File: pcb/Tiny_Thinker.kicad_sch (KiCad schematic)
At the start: 47 parts, among them J2 PERIPHERALS, J3 ADC_TIM, J8 USB_C_Receptacle_USB2.0_16P, SW1 SW_Push, SW2 SW_SPDT, U1 STM32F446RET6, U2 AMS1117-3.3, U3 TPS2116DRL, Y1 16MHz

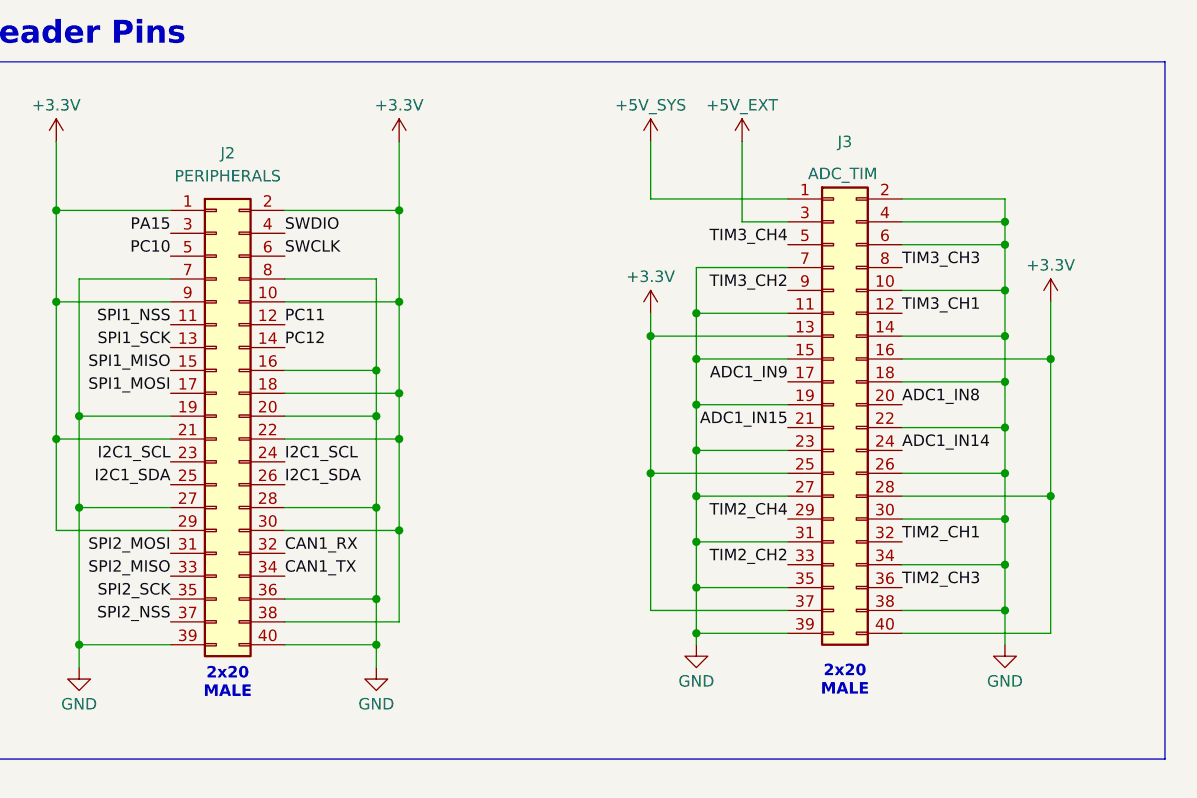
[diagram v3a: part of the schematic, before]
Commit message: renamed header connectors for BOM and connected NRST to a pin
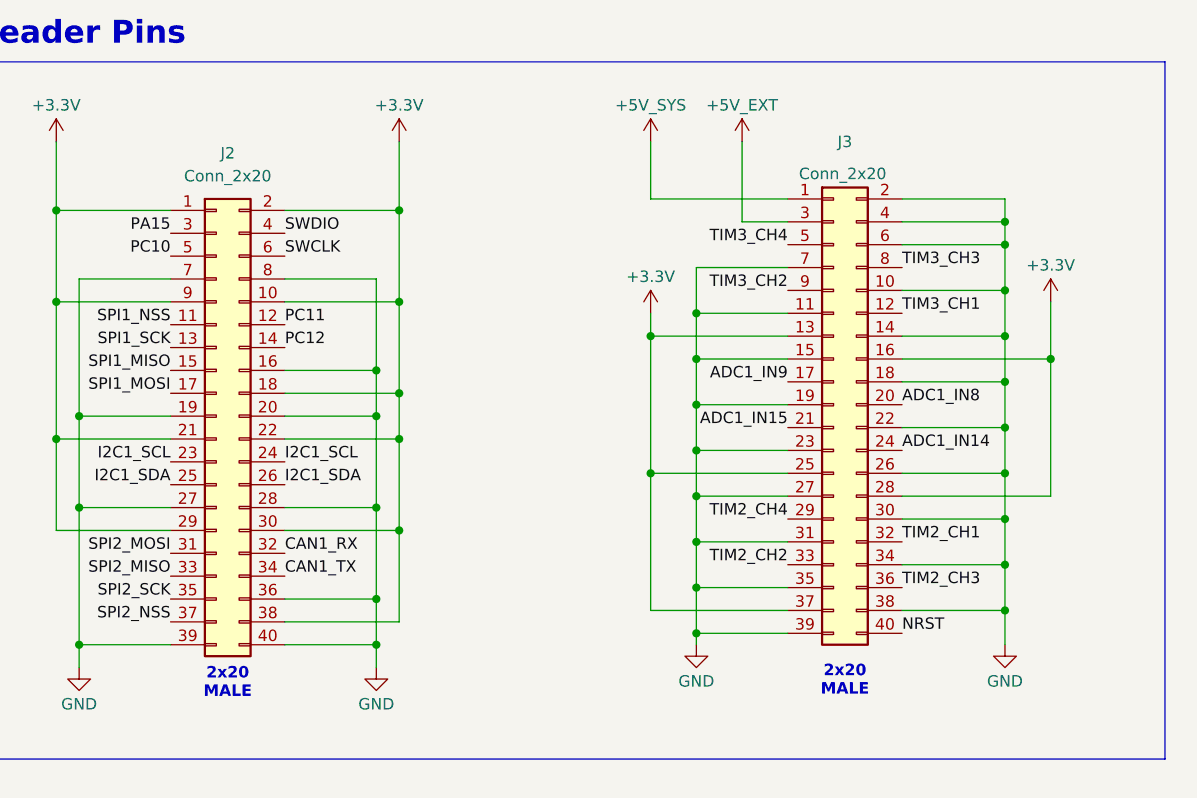
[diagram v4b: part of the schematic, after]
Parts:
- J2: value PERIPHERALS -> Conn_2x20
- J3: value ADC_TIM -> Conn_2x20
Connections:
- net +3.3V: no longer J3.40 (Pin_40)
- net NRST: now also J3.40 (Pin_40)
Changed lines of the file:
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@@
 	)
 	(junction
-		(at 369.57 205.74)
-		(diameter 0)
-		(color 0 0 0 0)
-	)
-	(junction
 		(at 259.08 184.15)
 		(diameter 0)
@@
 	(wire
 		(pts
-			(xy 369.57 220.98) (xy 369.57 205.74)
-		)
-		(stroke
-			(width 0)
-			(type default)
-		)
-	)
-	(wire
-		(pts
 			(xy 364.49 213.36) (xy 364.49 218.44)
 		)
@@
 	(wire
 		(pts
-			(xy 353.06 220.98) (xy 369.57 220.98)
-		)
-		(stroke
-			(width 0)
-			(type default)
-		)
-	)
-	(wire
-		(pts
 			(xy 294.64 222.25) (xy 294.64 224.79)
 		)
@@
 		)
 	)
+	(label "NRST"
+		(at 353.06 220.98 0)
+		(effects
+			(font
+				(size 1.27 1.27)
+			)
+			(justify left bottom)
+		)
+	)
 	(label "SWDIO"
 		(at 199.39 191.77 0)
@@
 			)
 		)
-		(property "Value" "ADC_TIM"
+		(property "Value" "Conn_2x20"
 			(at 346.456 169.926 0)
 			(effects
@@
 			)
 		)
-		(property "Value" "PERIPHERALS"
+		(property "Value" "Conn_2x20"
 			(at 278.13 170.18 0)
 			(effects

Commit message: updated gerbers
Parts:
- C10, C11: JLCPCB Part # C14445 -> C52923
- C12, C13: JLCPCB Part # C5674 -> C45783
- C14, C15: JLCPCB Part # C1545 -> C32949
- C18, C19, C20, C6: JLCPCB Part # C1691 -> C19702
- C9: JLCPCB Part # C1524 -> C15195
- U1: JLCPCB Part # C69336 -> C915971
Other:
- note removed: "try 470 Ohm"
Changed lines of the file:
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@@
 		)
 	)
-	(text "try\n470 Ohm"
-		(exclude_from_sim no)
-		(at 175.006 55.118 0)
-		(effects
-			(font
-				(size 1.27 1.27)
-				(thickness 0.254)
-				(bold yes)
-			)
-		)
-	)
 	(text "Mounting Holes"
 		(exclude_from_sim no)
@@
 			)
 		)
-		(property "JLCPCB Part #" "C5674"
+		(property "JLCPCB Part #" "C45783"
 			(at 111.76 54.61 0)
 			(effects
@@
 			)
 		)
-		(property "JLCPCB Part #" "C14445"
+		(property "JLCPCB Part #" "C52923"
 			(at 241.3 124.46 0)
 			(effects
@@
 			)
 		)
-		(property "JLCPCB Part #" "C14445"
+		(property "JLCPCB Part #" "C52923"
 			(at 210.82 124.46 0)
 			(effects
@@
 			)
 		)
-		(property "JLCPCB Part #" "C1691"
+		(property "JLCPCB Part #" "C19702"
 			(at 87.63 142.24 0)
 			(effects
@@
 			)
 		)
-		(property "JLCPCB Part #" "C1524"
+		(property "JLCPCB Part #" "C15195"
 			(at 198.12 124.46 0)
 			(effects
@@
 			)
 		)
-		(property "JLCPCB Part #" "C1691"
+		(property "JLCPCB Part #" "C19702"
 			(at 196.85 46.99 0)
 			(effects
@@
 			)
 		)
-		(property "JLCPCB Part #" "C1691"
+		(property "JLCPCB Part #" "C19702"
 			(at 264.16 46.99 0)
 			(effects
@@
 			)
 		)
-		(property "JLCPCB Part #" "C5674"
+		(property "JLCPCB Part #" "C45783"
 			(at 151.13 54.61 0)
 			(effects
@@
 			)
 		)
-		(property "JLCPCB Part #" "C69336"
+		(property "JLCPCB Part #" "C915971"
 			(at 179.07 199.39 0)
 			(effects
@@
 			)
 		)
-		(property "JLCPCB Part #" "C1691"
+		(property "JLCPCB Part #" "C19702"
 			(at 218.44 54.61 0)
 			(effects
@@
 			)
 		)
-		(property "JLCPCB Part #" "C1545"
+		(property "JLCPCB Part #" "C32949 "
 			(at 50.8 191.77 0)
 			(effects
@@
 			)
 		)
-		(property "JLCPCB Part #" "C1545"
+		(property "JLCPCB Part #" "C32949 "
 			(at 31.75 191.77 0)
 			(effects

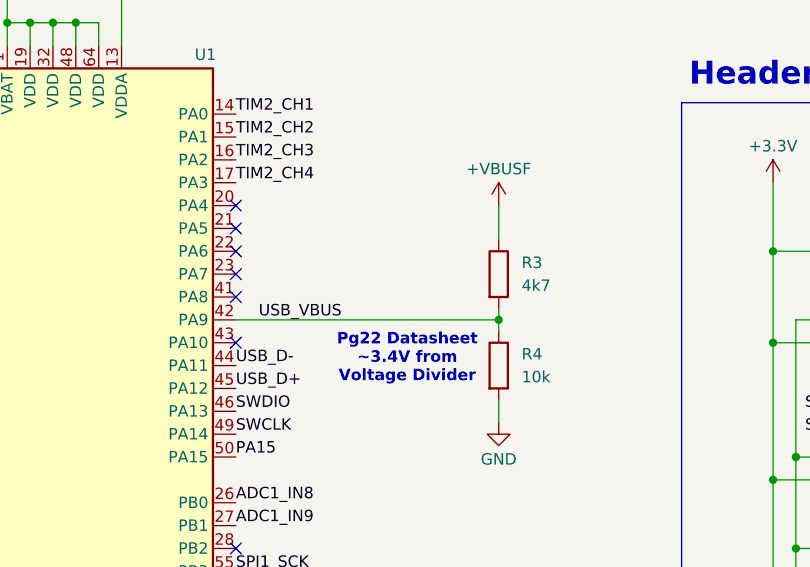
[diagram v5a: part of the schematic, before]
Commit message: added more comments to schematic
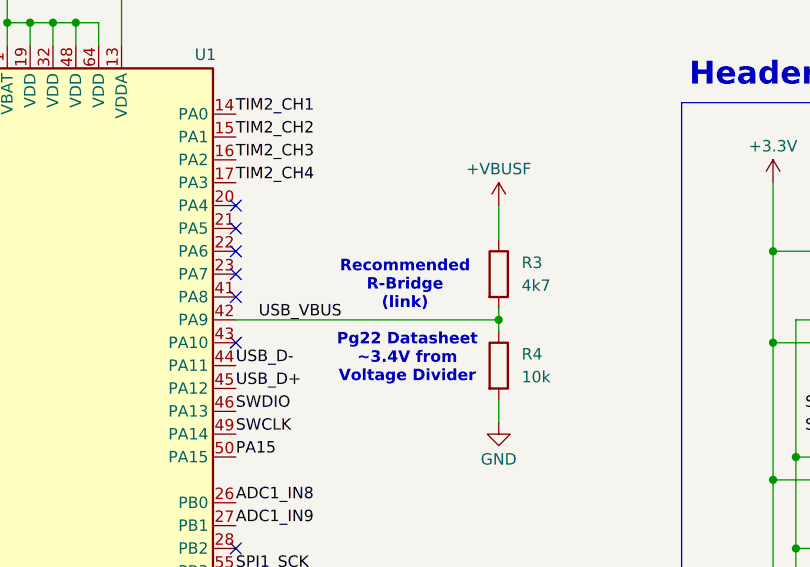
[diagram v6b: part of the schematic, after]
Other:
- note added: "Recommended R-Bridge (link)"
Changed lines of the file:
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@@
+		)
+	)
+	(text "Recommended\nR-Bridge\n(link)"
+		(exclude_from_sim no)
+		(at 218.186 177.8 0)
+		(effects
+			(font
+				(size 1.27 1.27)
+				(thickness 0.254)
+				(bold yes)
+			)
+			(href "https://community.st.com/t5/stm32-mcus/management-of-vbus-sensing-for-usb-device-design/ta-p/49485")
 		)
 	)

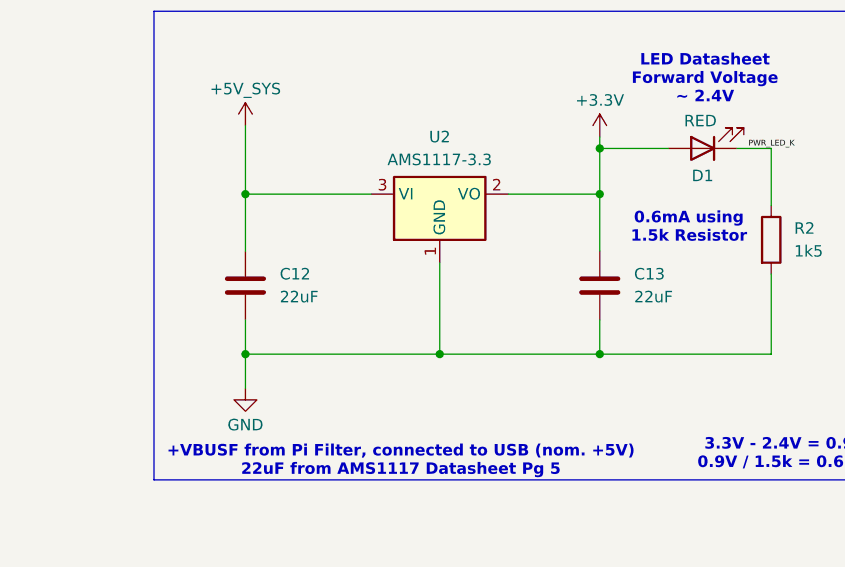
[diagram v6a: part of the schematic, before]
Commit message: changed AMS caps to tantalum per spec
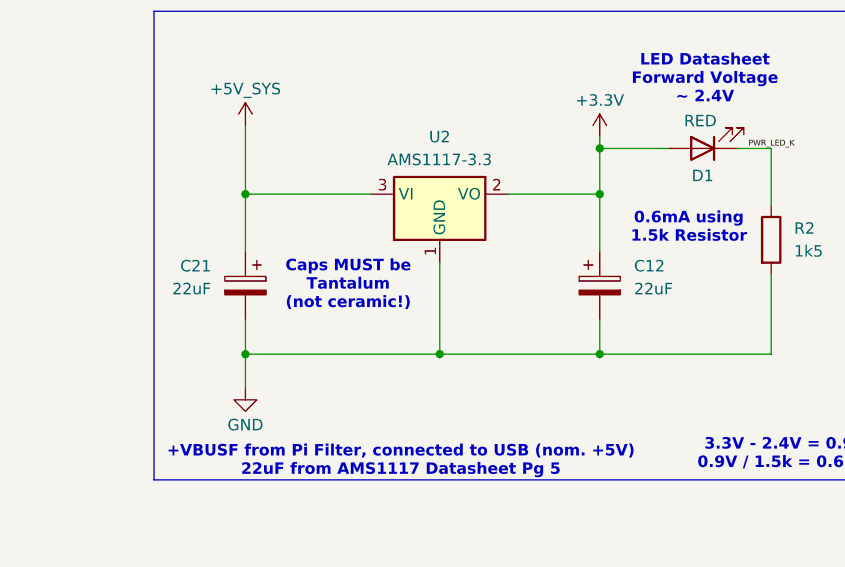
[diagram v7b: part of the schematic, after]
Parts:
- removed C12, C13: 22uF, Capacitor_SMD:C_0805_2012Metric, symbol Device:C
- added C12, C21: 22uF, Capacitor_Tantalum_SMD:CP_EIA-3216-18_Kemet-A, symbol Device:C_Polarized
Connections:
- net +3.3V: now also C12.1
- net +5V_SYS: now also C21.1
- net GND: now also C12.2, C21.2
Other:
- note added: "Caps MUST be Tantalum (not ceramic!)"
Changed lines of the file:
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@@
 		)
 	)
+	(text "Caps MUST be\nTantalum\n(not ceramic!)"
+		(exclude_from_sim no)
+		(at 123.19 54.61 0)
+		(effects
+			(font
+				(size 1.27 1.27)
+				(thickness 0.254)
+				(bold yes)
+			)
+		)
+	)
 	(text "Crystal Oscillator"
 		(exclude_from_sim no)
@@
 	)
 	(symbol
-		(lib_id "Device:C")
-		(at 111.76 54.61 0)
-		(unit 1)
-		(exclude_from_sim no)
-		(in_bom yes)
-		(on_board yes)
-		(dnp no)
-		(fields_autoplaced yes)
-		(property "Reference" "C12"
-			(at 115.57 53.3399 0)
-			(effects
-				(font
-					(size 1.27 1.27)
-				)
-				(justify left)
-			)
-		)
-		(property "Value" "22uF"
-			(at 115.57 55.8799 0)
-			(effects
-				(font
-					(size 1.27 1.27)
-				)
-				(justify left)
-			)
-		)
-		(property "Footprint" "Capacitor_SMD:C_0805_2012Metric"
-			(at 112.7252 58.42 0)
-			(effects
-				(font
-					(size 1.27 1.27)
-				)
-				(hide yes)
-			)
-		)
-		(property "Datasheet" "~"
-			(at 111.76 54.61 0)
-			(effects
-				(font
-					(size 1.27 1.27)
-				)
-				(hide yes)
-			)
-		)
-		(property "Description" "Unpolarized capacitor"
-			(at 111.76 54.61 0)
-			(effects
-				(font
-					(size 1.27 1.27)
-				)
-				(hide yes)
-			)
-		)
-		(property "JLCPCB Part #" "C45783"
-			(at 111.76 54.61 0)
-			(effects
-				(font
-					(size 1.27 1.27)
-				)
-				(hide yes)
-			)
-		)
-		(pin "1"
-		)
-		(pin "2"
-		)
-		(instances
-			(project "Tiny_Thinker"
-				(path "/1492d82e-cea7-4984-859f-7eb0a1e67ad8"
-					(reference "C12")
-					(unit 1)
-				)
-			)
-		)
-	)
-	(symbol
 		(lib_id "Mechanical:MountingHole")
 		(at 44.45 54.61 0)
@@
 	)
 	(symbol
+		(lib_id "Device:C_Polarized")
+		(at 151.13 54.61 0)
+		(unit 1)
+		(exclude_from_sim no)
+		(in_bom yes)
+		(on_board yes)
+		(dnp no)
+		(fields_autoplaced yes)
+		(property "Reference" "C12"
+			(at 154.94 52.4509 0)
+			(effects
+				(font
+					(size 1.27 1.27)
+				)
+				(justify left)
+			)
+		)
+		(property "Value" "22uF"
+			(at 154.94 54.9909 0)
+			(effects
+				(font
+					(size 1.27 1.27)
+				)
+				(justify left)
+			)
+		)
+		(property "Footprint" "Capacitor_Tantalum_SMD:CP_EIA-3216-18_Kemet-A"
+			(at 152.0952 58.42 0)
+			(effects
+				(font
+					(size 1.27 1.27)
+				)
+				(hide yes)
+			)
+		)
+		(property "Datasheet" "~"
+			(at 151.13 54.61 0)
+			(effects
+				(font
+					(size 1.27 1.27)
+				)
+				(hide yes)
+			)
+		)
+		(property "Description" "Polarized capacitor"
+			(at 151.13 54.61 0)
+			(effects
+				(font
+					(size 1.27 1.27)
+				)
+				(hide yes)
+			)
+		)
+		(property "JLCPCB Part #" " C11366"
+			(at 151.13 54.61 0)
+			(effects
+				(font
+					(size 1.27 1.27)
+				)
+				(hide yes)
+			)
+		)
+		(pin "2"
+		)
+		(pin "1"
+		)
+		(instances
+			(project "Tiny_Thinker"
+				(path "/1492d82e-cea7-4984-859f-7eb0a1e67ad8"
+					(reference "C12")
+					(unit 1)
+				)
+			)
+		)
+	)
+	(symbol
 		(lib_id "power:GND")
 		(at 241.3 133.35 0)
@@
 	)
 	(symbol
-		(lib_id "Device:C")
-		(at 151.13 54.61 0)
+		(lib_id "Device:C_Polarized")
+		(at 111.76 54.61 0)
+		(mirror y)
 		(unit 1)
 		(exclude_from_sim no)
@@
 		(on_board yes)
 		(dnp no)
-		(fields_autoplaced yes)
-		(property "Reference" "C13"
-			(at 154.94 53.3399 0)
+		(property "Reference" "C21"
+			(at 107.95 52.4509 0)
 			(effects
 				(font
@@
 		)
 		(property "Value" "22uF"
-			(at 154.94 55.8799 0)
+			(at 107.95 54.9909 0)
 			(effects
 				(font
@@
 			)
 		)
-		(property "Footprint" "Capacitor_SMD:C_0805_2012Metric"
-			(at 152.0952 58.42 0)
+		(property "Footprint" "Capacitor_Tantalum_SMD:CP_EIA-3216-18_Kemet-A"
+			(at 110.7948 58.42 0)
 			(effects
 				(font
@@
 		)
 		(property "Datasheet" "~"
-			(at 151.13 54.61 0)
+			(at 111.76 54.61 0)
 			(effects
 				(font
@@
 			)
 		)
-		(property "Description" "Unpolarized capacitor"
-			(at 151.13 54.61 0)
+		(property "Description" "Polarized capacitor"
+			(at 111.76 54.61 0)
 			(effects
 				(font
@@
 			)
 		)
-		(property "JLCPCB Part #" "C45783"
-			(at 151.13 54.61 0)
+		(property "JLCPCB Part #" " C11366"
+			(at 111.76 54.61 0)
 			(effects
 				(font
@@
 			)
 		)
-		(pin "1"
-		)
 		(pin "2"
 		)
+		(pin "1"
+		)
 		(instances
-			(project "Tiny_Thinker"
+			(project ""
 				(path "/1492d82e-cea7-4984-859f-7eb0a1e67ad8"
-					(reference "C13")
+					(reference "C21")
 					(unit 1)
 				)

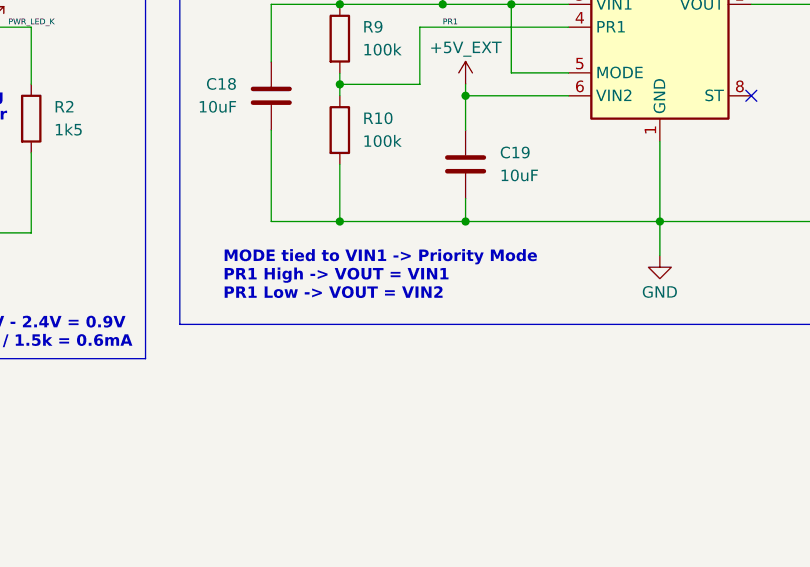
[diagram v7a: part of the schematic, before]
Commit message: comments on TPS2116
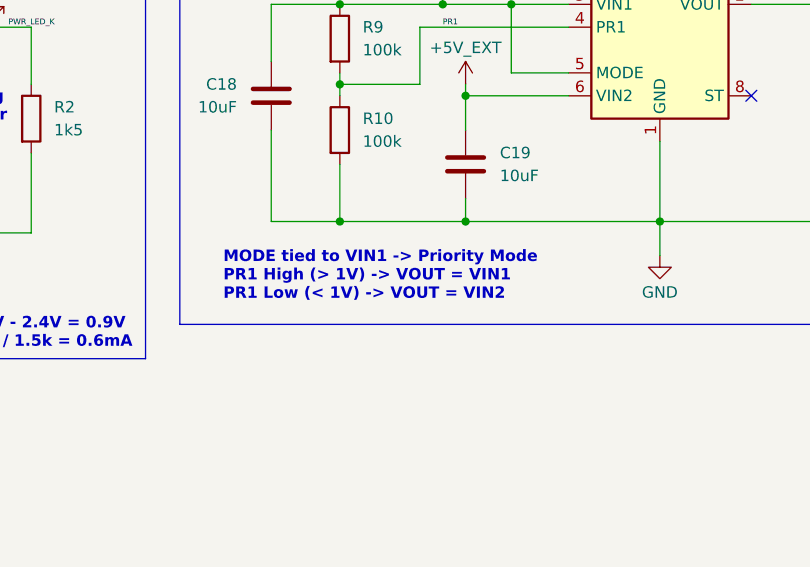
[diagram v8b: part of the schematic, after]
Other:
- note added: "MODE tied to VIN1 -> Priority Mode PR1 High (> 1V) -> VOUT = VIN1 PR1 Low (< 1V) -> VOUT = VIN2"
- note removed: "MODE tied to VIN1 -> Priority Mode PR1 High -> VOUT = VIN1 PR1 Low -> VOUT = VIN2"
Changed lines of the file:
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@@
 		)
 	)
-	(text "MODE tied to VIN1 -> Priority Mode\nPR1 High -> VOUT = VIN1\nPR1 Low -> VOUT = VIN2"
+	(text "MODE tied to VIN1 -> Priority Mode\nPR1 High (> 1V) -> VOUT = VIN1\nPR1 Low (< 1V) -> VOUT = VIN2"
 		(exclude_from_sim no)
 		(at 191.516 67.056 0)
